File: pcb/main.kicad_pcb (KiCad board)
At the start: 2 copper layers, 3 parts, among them Q1 BC337

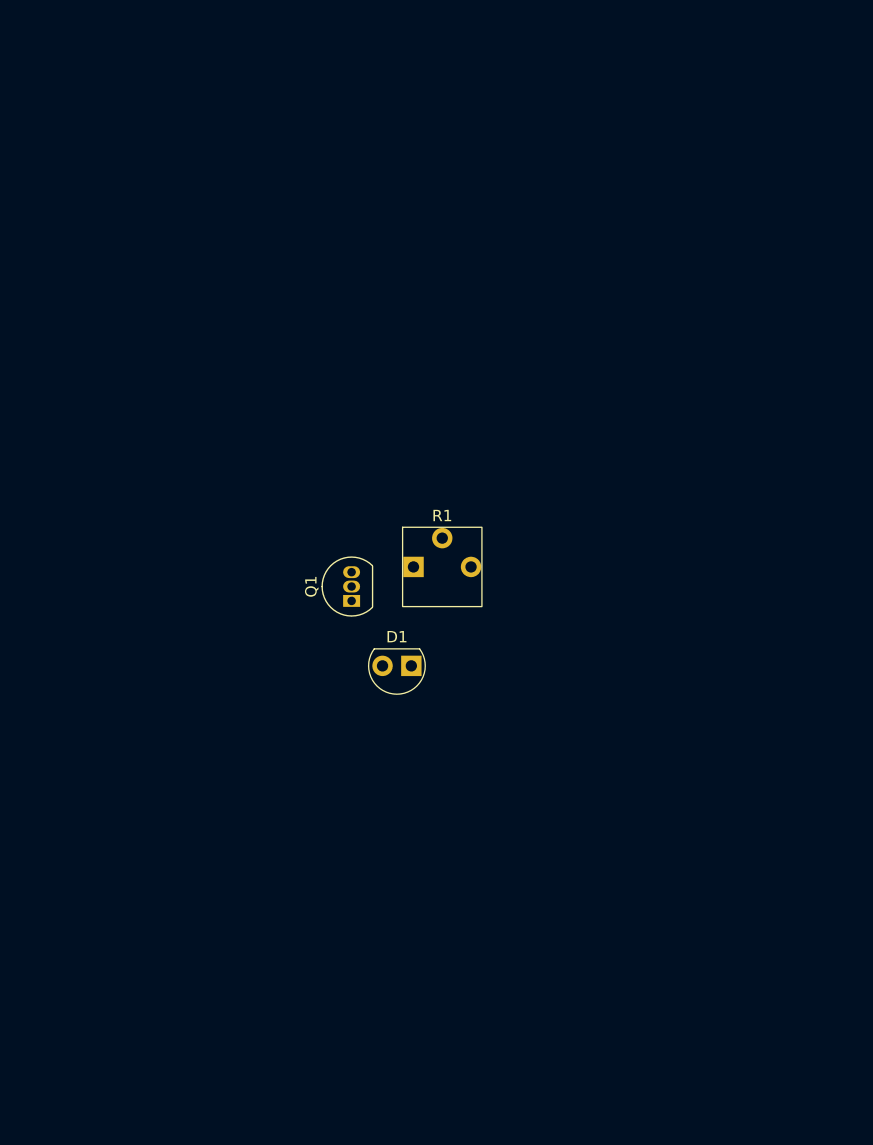
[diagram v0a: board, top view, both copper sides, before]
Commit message: Added edge cuts and a model hand for size reference.
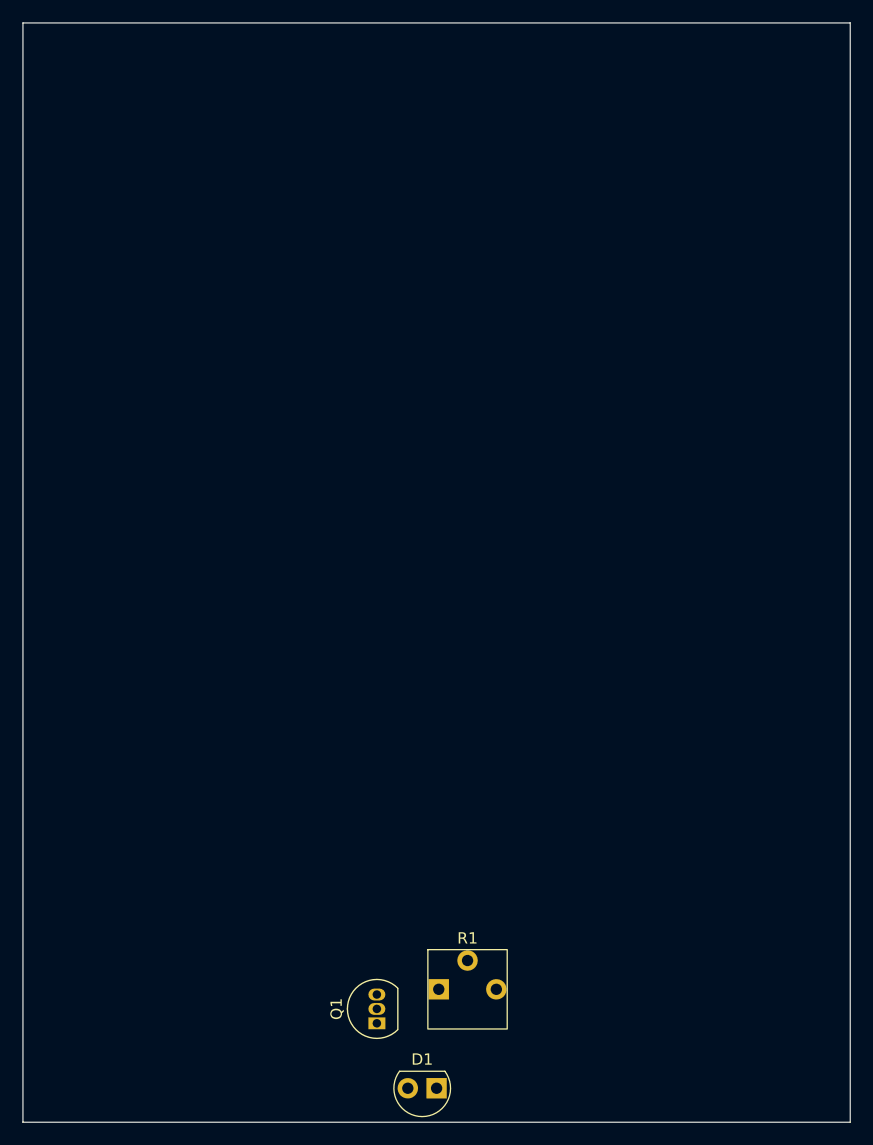
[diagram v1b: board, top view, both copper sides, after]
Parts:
- added N1: Housing, deps:Housing - main, F.Cu at (145.0, 100.0)
- moved Q1 37.3 mm to (139.2, 145.3)
- moved R1 37.3 mm to (147.2, 142.3)
- moved D1 37.3 mm to (143.2, 151.0)
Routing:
- added copper zone on In1.Cu, net GND
- added copper zone on In2.Cu, net GND
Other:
- board outline added: 73 x 97 mm
- copper layers 2 -> 4
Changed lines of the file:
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@@
 	(layers
 		(0 "F.Cu" signal)
+		(4 "In1.Cu" power)
+		(6 "In2.Cu" power)
 		(2 "B.Cu" signal)
 		(9 "F.Adhes" user "F.Adhesive")
@@
 	)
 	(setup
+		(stackup
+			(layer "F.SilkS"
+				(type "Top Silk Screen")
+			)
+			(layer "F.Paste"
+				(type "Top Solder Paste")
+			)
+			(layer "F.Mask"
+				(type "Top Solder Mask")
+				(thickness 0.01)
+			)
+			(layer "F.Cu"
+				(type "copper")
+				(thickness 0.035)
+			)
+			(layer "dielectric 1"
+				(type "prepreg")
+				(thickness 0.1)
+				(material "FR4")
+				(epsilon_r 4.5)
+				(loss_tangent 0.02)
+			)
+			(layer "In1.Cu"
+				(type "copper")
+				(thickness 0.035)
+			)
+			(layer "dielectric 2"
+				(type "core")
+				(thickness 1.24)
+				(material "FR4")
+				(epsilon_r 4.5)
+				(loss_tangent 0.02)
+			)
+			(layer "In2.Cu"
+				(type "copper")
+				(thickness 0.035)
+			)
+			(layer "dielectric 3"
+				(type "prepreg")
+				(thickness 0.1)
+				(material "FR4")
+				(epsilon_r 4.5)
+				(loss_tangent 0.02)
+			)
+			(layer "B.Cu"
+				(type "copper")
+				(thickness 0.035)
+			)
+			(layer "B.Mask"
+				(type "Bottom Solder Mask")
+				(thickness 0.01)
+			)
+			(layer "B.Paste"
+				(type "Bottom Solder Paste")
+			)
+			(layer "B.SilkS"
+				(type "Bottom Silk Screen")
+			)
+			(copper_finish "None")
+			(dielectric_constraints no)
+		)
 		(pad_to_mask_clearance 0)
 		(allow_soldermask_bridges_in_footprints no)
 		(tenting front back)
+		(aux_axis_origin 145 100)
+		(grid_origin 145 100)
 		(pcbplotparams
 			(layerselection 0x00000000_00000000_55555555_5755f5ff)
@@
 	(footprint "deps:LTR-516AD"
 		(layer "F.Cu")
-		(at 141 113.73)
+		(at 143.23 151)
 		(descr "SENSOR PHOTODIODE 940NM RADIAL")
 		(property "Reference" "D1"
@@
 	(footprint "deps:Trimmer 3362P"
 		(layer "F.Cu")
-		(at 145 105)
+		(at 147.23 142.27)
 		(property "Reference" "R1"
 			(at 0 -4.5 0)
@@
 	(footprint "Package_TO_SOT_THT:TO-92_Inline"
 		(layer "F.Cu")
-		(at 137 108 90)
+		(at 139.23 145.27 90)
 		(descr "TO-92 leads in-line, narrow, oval pads, drill 0.75mm (see NXP sot054_po.pdf)")
 		(tags "to-92 sc-43 sc-43a sot54 PA33 transistor")
@@
 			)
 		)
+	)
+	(footprint "deps:Housing - main"
+		(locked yes)
+		(layer "F.Cu")
+		(at 145 100)
+		(property "Reference" "N1"
+			(at 0 -0.5 0)
+			(unlocked yes)
+			(layer "F.SilkS")
+			(hide yes)
+			(effects
+				(font
+					(size 1 1)
+					(thickness 0.1)
+				)
+			)
+		)
+		(property "Value" "Housing"
+			(at 0 1 0)
+			(unlocked yes)
+			(layer "F.Fab")
+			(hide yes)
+			(effects
+				(font
+					(size 1 1)
+					(thickness 0.15)
+				)
+			)
+		)
+		(property "Datasheet" ""
+			(at 0 0 0)
+			(unlocked yes)
+			(layer "F.Fab")
+			(hide yes)
+			(effects
+				(font
+					(size 1 1)
+					(thickness 0.15)
+				)
+			)
+		)
+		(property "Description" "Housing"
+			(at 0 0 0)
+			(unlocked yes)
+			(layer "F.Fab")
+			(hide yes)
+			(effects
+				(font
+					(size 1 1)
+					(thickness 0.15)
+				)
+			)
+		)
+		(property ki_fp_filters "Enclosure* Housing*")
+		(sheetname "/")
+		(sheetfile "main.kicad_sch")
+		(fp_line
+			(start -0.5 -0.5)
+			(end 0.5 0.5)
+			(stroke
+				(width 0.1)
+				(type default)
+			)
+			(layer "User.4")
+		)
+		(fp_line
+			(start 0.5 -0.5)
+			(end -0.5 0.5)
+			(stroke
+				(width 0.1)
+				(type default)
+			)
+			(layer "User.4")
+		)
+		(fp_circle
+			(center 0 0)
+			(end 0.5 -0.5)
+			(stroke
+				(width 0.1)
+				(type solid)
+			)
+			(fill no)
+			(layer "User.4")
+		)
+		(embedded_fonts no)
+		(model "${KIPRJMOD}/../deps/pcb/Hand.step"
+			(opacity 0.5200)
+			(offset
+				(xyz 0 0 -19)
+			)
+			(scale
+				(xyz 1 1 1)
+			)
+			(rotate
+				(xyz -0 -180 -0)
+			)
+		)
+		(model "${KIPRJMOD}/../data/main.step"
+			(hide yes)
+			(offset
+				(xyz 0 0 -1.6)
+			)
+			(scale
+				(xyz 1 1 1)
+			)
+			(rotate
+				(xyz -0 -0 -0)
+			)
+		)
+	)
+	(gr_rect
+		(start 108 57)
+		(end 181 154)
+		(stroke
+			(width 0.05)
+			(type default)
+		)
+		(fill no)
+		(layer "Edge.Cuts")
+	)
+	(zone
+		(net 4)
+		(net_name "GND")
+		(layers "In1.Cu" "In2.Cu")
+		(hatch edge 0.5)
+		(connect_pads
+			(clearance 0.5)
+		)
+		(min_thickness 0.25)
+		(filled_areas_thickness no)
+		(fill yes
+			(thermal_gap 0.5)
+			(thermal_bridge_width 0.5)
+		)
+		(polygon
+			(pts
+				(xy 66 28.5) (xy 227 28.5) (xy 227 161.5) (xy 66 161.5)
+			)
+		)

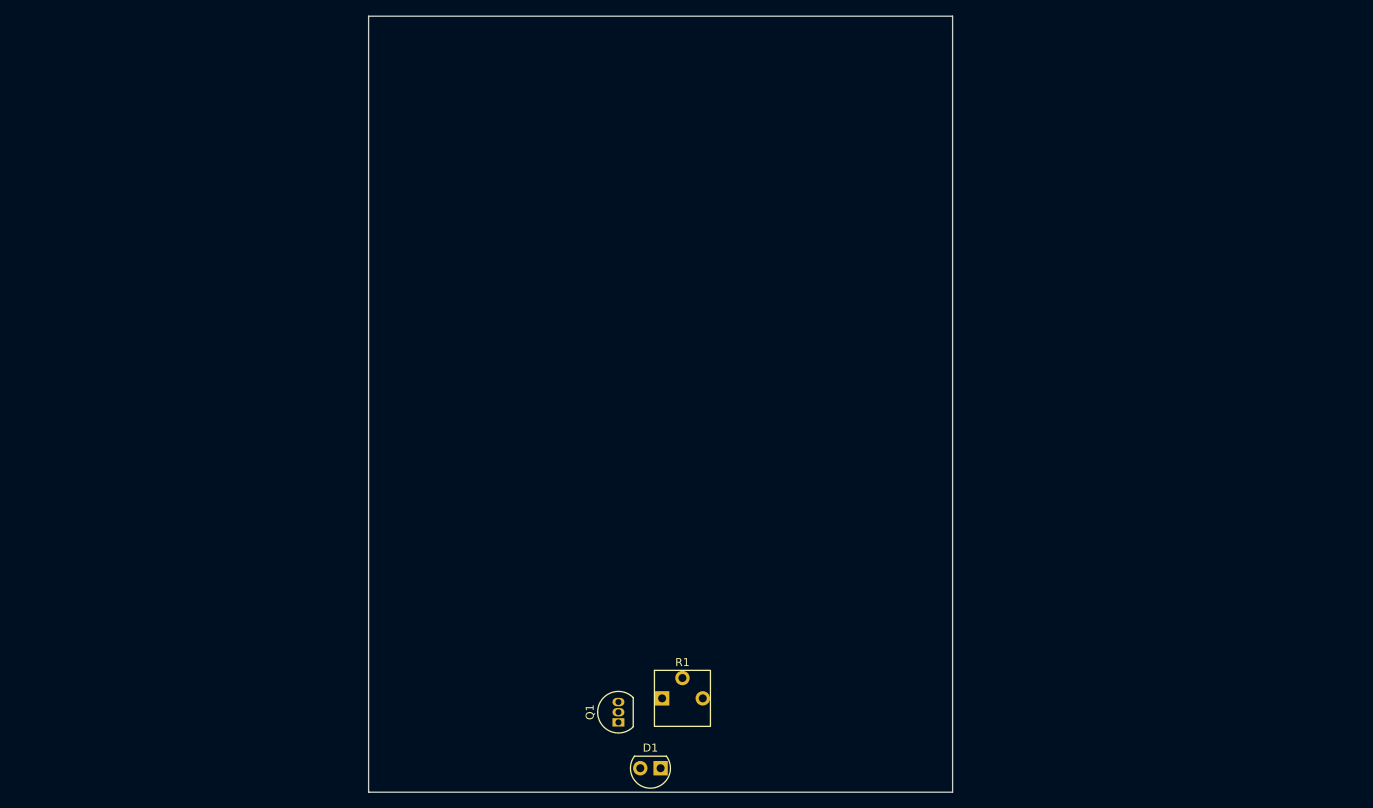
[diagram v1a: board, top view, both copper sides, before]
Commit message: Laid out first stages.
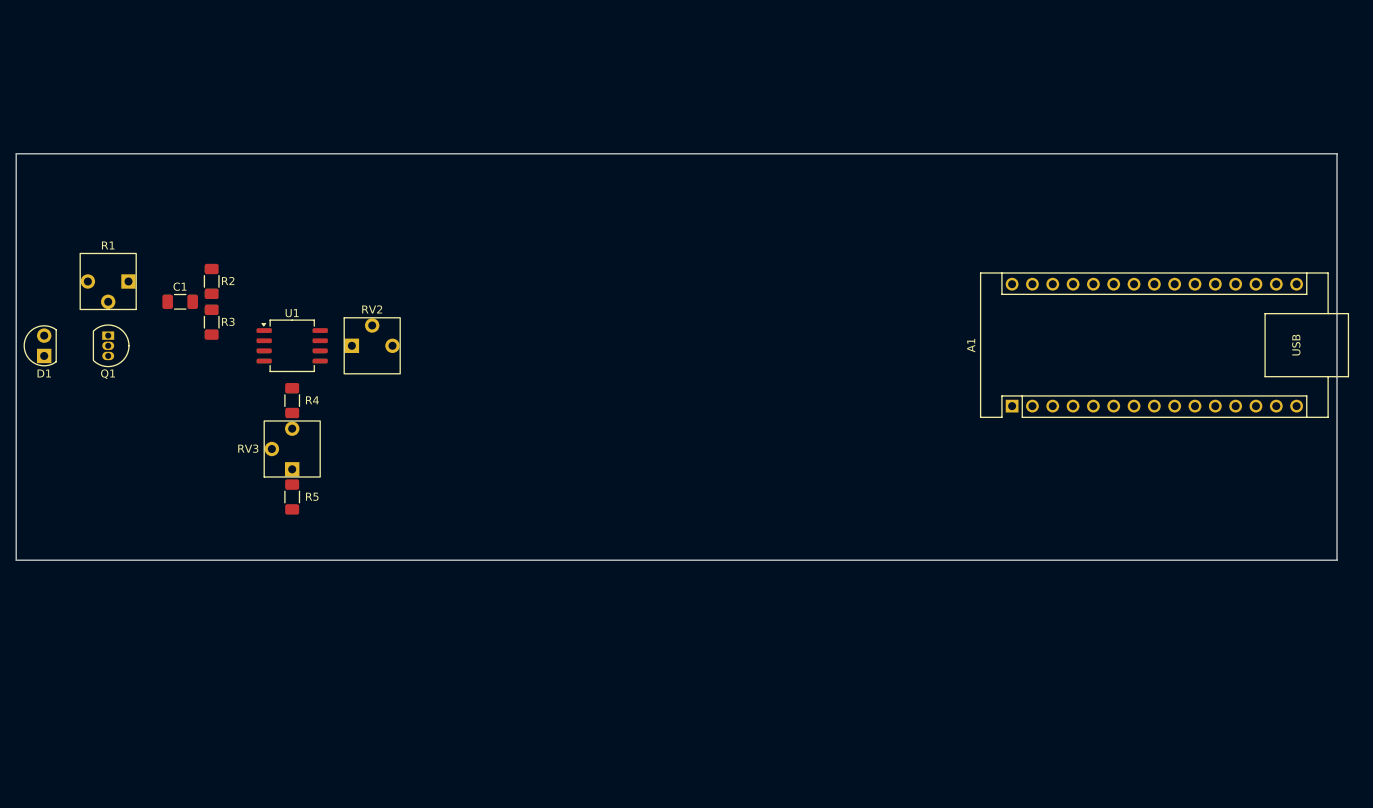
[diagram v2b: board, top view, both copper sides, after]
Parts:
- added A1: Arduino_Nano_v3.x, deps:Arduino_Nano, F.Cu at (188.4, 105.7)
- added C1: 1n, Capacitor_SMD:C_1206_3216Metric_Pad1.33x1.80mm_HandSolder, F.Cu at (84.5, 92.7)
- added R2: 680k, Resistor_SMD:R_1206_3216Metric_Pad1.30x1.75mm_HandSolder, F.Cu at (88.4, 90.1)
- added R3: 1M, Resistor_SMD:R_1206_3216Metric_Pad1.30x1.75mm_HandSolder, F.Cu at (88.4, 95.3)
- added R4: 680, Resistor_SMD:R_1206_3216Metric_Pad1.30x1.75mm_HandSolder, F.Cu at (98.5, 105.0)
- added R5: 330, Resistor_SMD:R_1206_3216Metric_Pad1.30x1.75mm_HandSolder, F.Cu at (98.5, 117.1)
- added RV2: 100k, deps:Potentiometer 3362P, F.Cu at (108.5, 98.2)
- added RV3: 100k, deps:Potentiometer 3362P, F.Cu at (98.5, 111.1)
- added U1: LM358, Package_SO:SOIC-8_5.3x6.2mm_P1.27mm, F.Cu at (98.5, 98.2)
- moved D1 92.4 mm to (67.5, 98.2), turned to -90 degrees
- moved R1 88.7 mm to (75.5, 90.2), turned to 180 degrees
- moved Q1 80.0 mm to (75.5, 96.9), turned to -90 degrees
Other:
- board size 73 x 97 mm -> 165.1 x 50.8 mm
- board text added: "Phuc Doan phucxdoan@gmail.com phucxdoan@vt.edu github.com/PhucXDoan 628-999-3600"

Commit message: Placed all components.
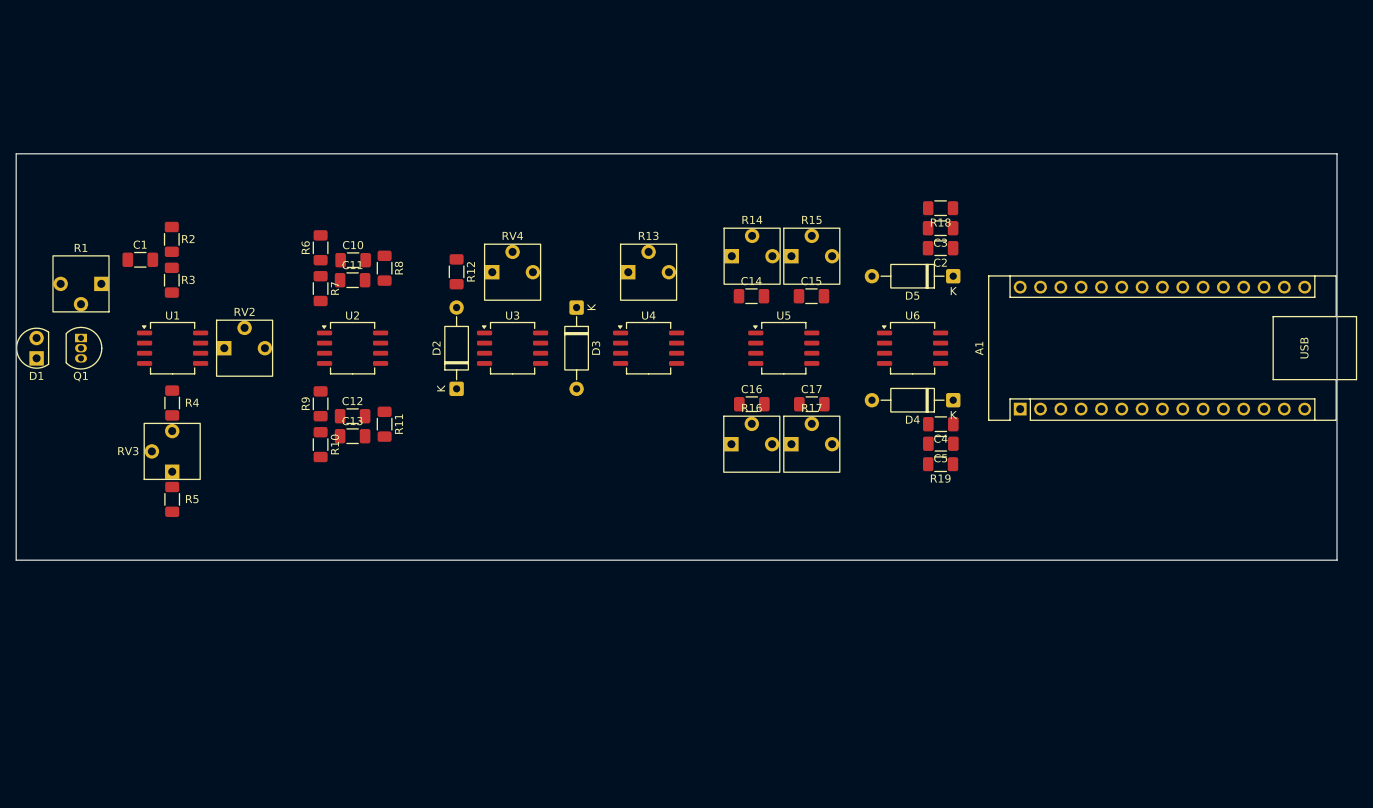
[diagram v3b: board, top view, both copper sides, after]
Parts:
- added C10: 4n7, Capacitor_SMD:C_1206_3216Metric_Pad1.33x1.80mm_HandSolder, F.Cu at (106.1, 87.5)
- added C11: 4n7, Capacitor_SMD:C_1206_3216Metric_Pad1.33x1.80mm_HandSolder, F.Cu at (106.0, 90.0)
- added C12: 4n7, Capacitor_SMD:C_1206_3216Metric_Pad1.33x1.80mm_HandSolder, F.Cu at (106.0, 107.0)
- added C13: 4n7, Capacitor_SMD:C_1206_3216Metric_Pad1.33x1.80mm_HandSolder, F.Cu at (106.0, 109.5)
- added C14: 1u, Capacitor_SMD:C_1206_3216Metric_Pad1.33x1.80mm_HandSolder, F.Cu at (155.9, 92.0)
- added C15: 1n, Capacitor_SMD:C_1206_3216Metric_Pad1.33x1.80mm_HandSolder, F.Cu at (163.4, 92.0)
- added C16: 1u, Capacitor_SMD:C_1206_3216Metric_Pad1.33x1.80mm_HandSolder, F.Cu at (155.9, 105.5)
- added C17: 4n7, Capacitor_SMD:C_1206_3216Metric_Pad1.33x1.80mm_HandSolder, F.Cu at (163.4, 105.5)
- added C2: 1u, Capacitor_SMD:C_1206_3216Metric_Pad1.33x1.80mm_HandSolder, F.Cu at (179.5, 86.0)
- added C3: 1u, Capacitor_SMD:C_1206_3216Metric_Pad1.33x1.80mm_HandSolder, F.Cu at (179.5, 83.5)
- added C4: 1u, Capacitor_SMD:C_1206_3216Metric_Pad1.33x1.80mm_HandSolder, F.Cu at (179.5, 108.0)
- added C5: 1u, Capacitor_SMD:C_1206_3216Metric_Pad1.33x1.80mm_HandSolder, F.Cu at (179.5, 110.4)
- added D2: 1N5817, Diode_THT:D_A-405_P10.16mm_Horizontal, F.Cu at (119.0, 103.6)
- added D3: 1N5817, Diode_THT:D_A-405_P10.16mm_Horizontal, F.Cu at (134.0, 93.4)
- added D4: 1N5817, Diode_THT:D_A-405_P10.16mm_Horizontal, F.Cu at (181.1, 105.0)
- added D5: 1N5817, Diode_THT:D_A-405_P10.16mm_Horizontal, F.Cu at (181.1, 89.5)
- added R10: 15k, Resistor_SMD:R_1206_3216Metric_Pad1.30x1.75mm_HandSolder, F.Cu at (102.0, 110.6)
- added R11: 33k, Resistor_SMD:R_1206_3216Metric_Pad1.30x1.75mm_HandSolder, F.Cu at (110.0, 108.0)
- added R12: 1k, Resistor_SMD:R_1206_3216Metric_Pad1.30x1.75mm_HandSolder, F.Cu at (119.0, 88.9)
- added R13: 100k, deps:Trimmer 3362P, F.Cu at (143.0, 89.0)
- added R14: 100k, deps:Trimmer 3362P, F.Cu at (155.9, 87.0)
- added R15: 100k, deps:Trimmer 3362P, F.Cu at (163.4, 87.0)
- added R16: 100k, deps:Trimmer 3362P, F.Cu at (155.9, 110.5)
- added R17: 100k, deps:Trimmer 3362P, F.Cu at (163.4, 110.5)
- added R18: 100k, Resistor_SMD:R_1206_3216Metric_Pad1.30x1.75mm_HandSolder, F.Cu at (179.5, 81.0)
- added R19: 100k, Resistor_SMD:R_1206_3216Metric_Pad1.30x1.75mm_HandSolder, F.Cu at (179.5, 113.0)
- added R6: 15k, Resistor_SMD:R_1206_3216Metric_Pad1.30x1.75mm_HandSolder, F.Cu at (102.0, 85.9)
- added R7: 15k, Resistor_SMD:R_1206_3216Metric_Pad1.30x1.75mm_HandSolder, F.Cu at (102.0, 91.1)
- added R8: 33k, Resistor_SMD:R_1206_3216Metric_Pad1.30x1.75mm_HandSolder, F.Cu at (110.0, 88.5)
- added R9: 15k, Resistor_SMD:R_1206_3216Metric_Pad1.30x1.75mm_HandSolder, F.Cu at (102.0, 105.4)
- added RV4: 1k, deps:Potentiometer 3362P, F.Cu at (126.0, 89.0)
- added U2: LM358, Package_SO:SOIC-8_5.3x6.2mm_P1.27mm, F.Cu at (106.0, 98.5)
- added U3: LM358, Package_SO:SOIC-8_5.3x6.2mm_P1.27mm, F.Cu at (126.0, 98.5)
- added U4: LM358, Package_SO:SOIC-8_5.3x6.2mm_P1.27mm, F.Cu at (143.0, 98.5)
- added U5: LM358, Package_SO:SOIC-8_5.3x6.2mm_P1.27mm, F.Cu at (159.9, 98.5)
- added U6: LM358, Package_SO:SOIC-8_5.3x6.2mm_P1.27mm, F.Cu at (176.0, 98.5)
- moved RV2 16.0 mm to (92.5, 98.5)
- moved R4 15.0 mm to (83.5, 105.4)
- moved R5 15.0 mm to (83.5, 117.4)
- moved RV3 15.0 mm to (83.5, 111.4)
- moved U1 15.0 mm to (83.5, 98.5)
- moved C1 7.24 mm to (79.5, 87.4)
- moved R2 7.24 mm to (83.4, 84.9)
- moved R3 7.24 mm to (83.4, 90.0)
- moved Q1 3.41 mm to (72.0, 97.2)
- moved R1 3.41 mm to (72.0, 90.5)
- moved A1 1.08 mm to (189.4, 106.1)
- moved D1 1.00 mm to (66.5, 98.5)
